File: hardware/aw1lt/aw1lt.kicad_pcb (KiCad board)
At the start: 2 copper layers, 30 x 22 mm, 27 parts, among them J1 ISP_FTDI, Q1 Q_NPN_CBE, SW1 SW_Push, SW2 SW_Push, SW3 SW_Push, U1 DS3231MZ, U2 ATMEGA328P-AU

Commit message: still trying to figure out this routing and placement...
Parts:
- C2, C3, C4, C7, R2: moved to B.Cu
- moved C9 15.0 mm to (126.6, 128.6)
- moved C8 12.5 mm to (127.4, 131.6), turned to 180 degrees
- moved C1 11.1 mm to (152.4, 137.2), turned to 180 degrees
- moved C10 10.8 mm to (126.2, 140.8)
- moved C3 8.94 mm to (148.2, 145.8), turned to 180 degrees
- moved C4 8.62 mm to (139.2, 145.8), turned to 180 degrees
- moved R2 8.30 mm to (132.4, 145.6)
- moved C2 8.20 mm to (144.4, 145.8)
- moved C7 7.79 mm to (127.2, 144.4), turned to 90 degrees
- moved R1 6.00 mm to (145.2, 131.8), turned to 0 degrees
- moved C6 3.20 mm to (127.2, 141.8), turned to 270 degrees
- moved U2 1.61 mm to (135.2, 132.4), turned to 0 degrees
- moved SW3 1.60 mm to (152.6, 142.0)
- moved SW1 1.00 mm to (127.4, 136.0)
- moved RN1 1.00 mm to (143.8, 135.2)
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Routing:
- net SCL: track 13.7 -> 0.00 mm
- net PB0: track 13.5 -> 0.00 mm
- net SDA: track 13.1 -> 0.00 mm
- net Net-(C6-Pad1): track 0.00 -> 7.65 mm
- net Net-(C2-Pad2): track 0.00 -> 7.48 mm, vias 0 -> 1
- net Net-(C2-Pad1): track 0.00 -> 6.35 mm, vias 0 -> 1
- net INT0: track 5.00 -> 0.00 mm
- net Net-(C3-Pad2): track 0.00 -> 4.96 mm, vias 0 -> 1
- net Net-(C3-Pad1): track 0.00 -> 4.54 mm, vias 0 -> 1
- net PB1: track 2.20 -> 0.00 mm
- net PB2: track 2.23 -> 0.11 mm

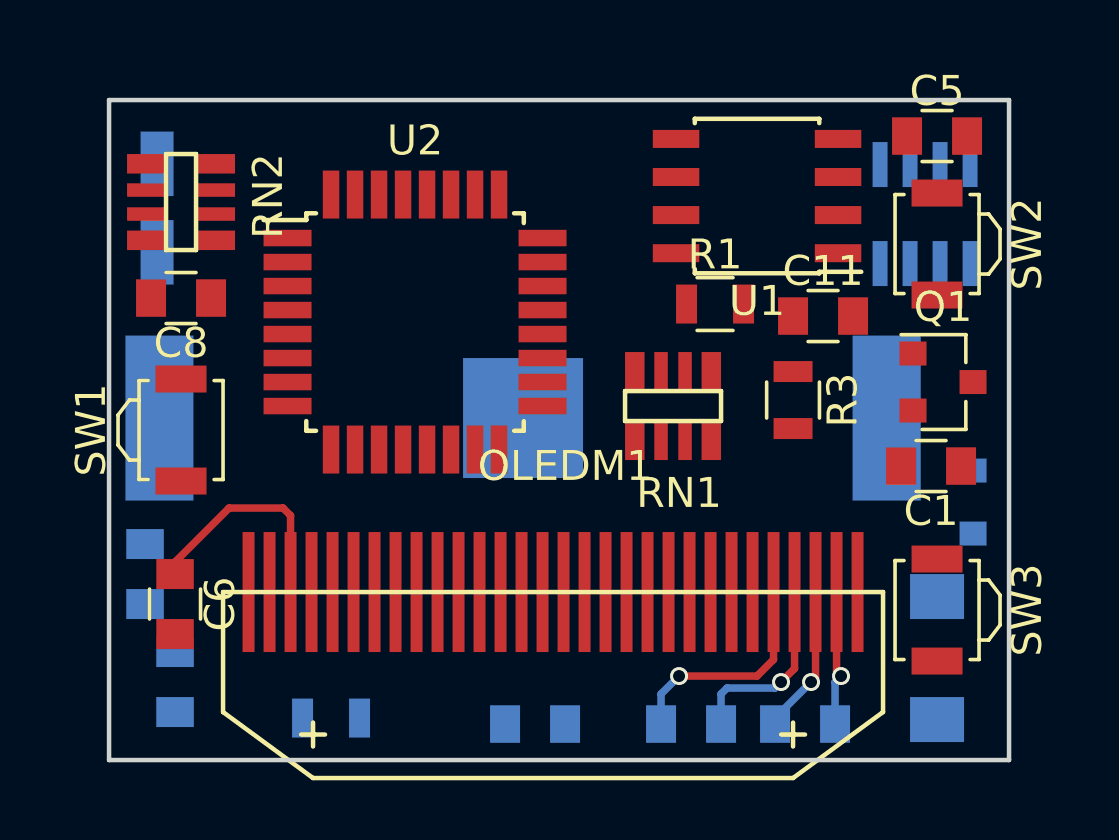
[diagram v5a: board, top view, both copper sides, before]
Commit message: made the coin cell footprint more accurate, did some measurements so that i know how far the actual coin battery will be protruding from the retainer and where i can place components
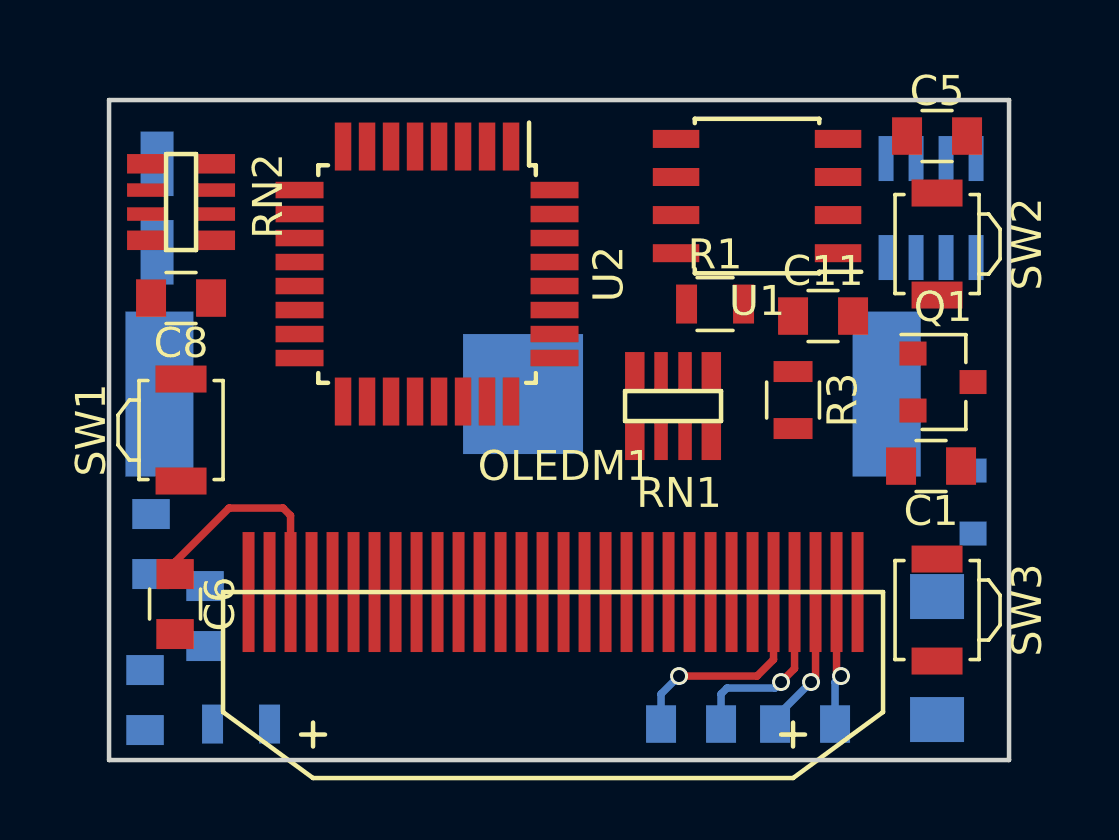
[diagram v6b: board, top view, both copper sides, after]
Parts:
- moved C4 11.6 mm to (128.2, 142.2), turned to 270 degrees
- moved R2 3.01 mm to (129.4, 145.8), turned to 180 degrees
- moved U2 1.65 mm to (135.6, 130.8), turned to 270 degrees
- moved C7 1.17 mm to (126.2, 145.0), turned to 270 degrees
- moved C10 1.02 mm to (126.4, 139.8)
- moved BT1 0.80 mm to (138.8, 134.8), turned to 180 degrees
- moved J1 0.28 mm to (152.4, 128.6)

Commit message: working on routing
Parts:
- moved C4 26.7 mm to (153.8, 134.6)
- moved R3 1.08 mm to (148.2, 136.0)
- moved C11 1.02 mm to (149.0, 133.2)
- moved RN1 0.72 mm to (144.2, 135.8)
- moved C7 0.45 mm to (126.4, 144.6)
- moved C2 0.40 mm to (144.8, 145.8)
- moved C3 0.40 mm to (148.6, 145.8)
- moved C10 0.28 mm to (126.2, 140.0)
- moved R1 0.20 mm to (145.4, 131.8)
- moved R2 0.20 mm to (129.4, 145.6)
- moved C8 0.20 mm to (127.2, 131.6)
- moved U1 0.20 mm to (146.6, 128.0)
- turned C9 to 90 degrees
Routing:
- net INT0: track 0.00 -> 16.0 mm, vias 0 -> 2
- net SPKR: track 0.00 -> 13.2 mm
- net Net-(C11-Pad1): track 0.00 -> 13.1 mm, vias 0 -> 3
- net SDA: track 0.00 -> 12.5 mm, vias 0 -> 2
- net SCL: track 0.00 -> 10.0 mm
- net Net-(C2-Pad2): track 7.48 -> 0.00 mm, vias 1 -> 0
- net Net-(C2-Pad1): track 6.35 -> 0.00 mm, vias 1 -> 0
- net Net-(C3-Pad2): track 4.96 -> 0.00 mm, vias 1 -> 0
- net Net-(C3-Pad1): track 4.54 -> 0.00 mm, vias 1 -> 0
- net PB2: track 0.11 -> 2.94 mm
- net PB1: track 0.00 -> 2.80 mm
- net PB0: track 0.00 -> 2.80 mm

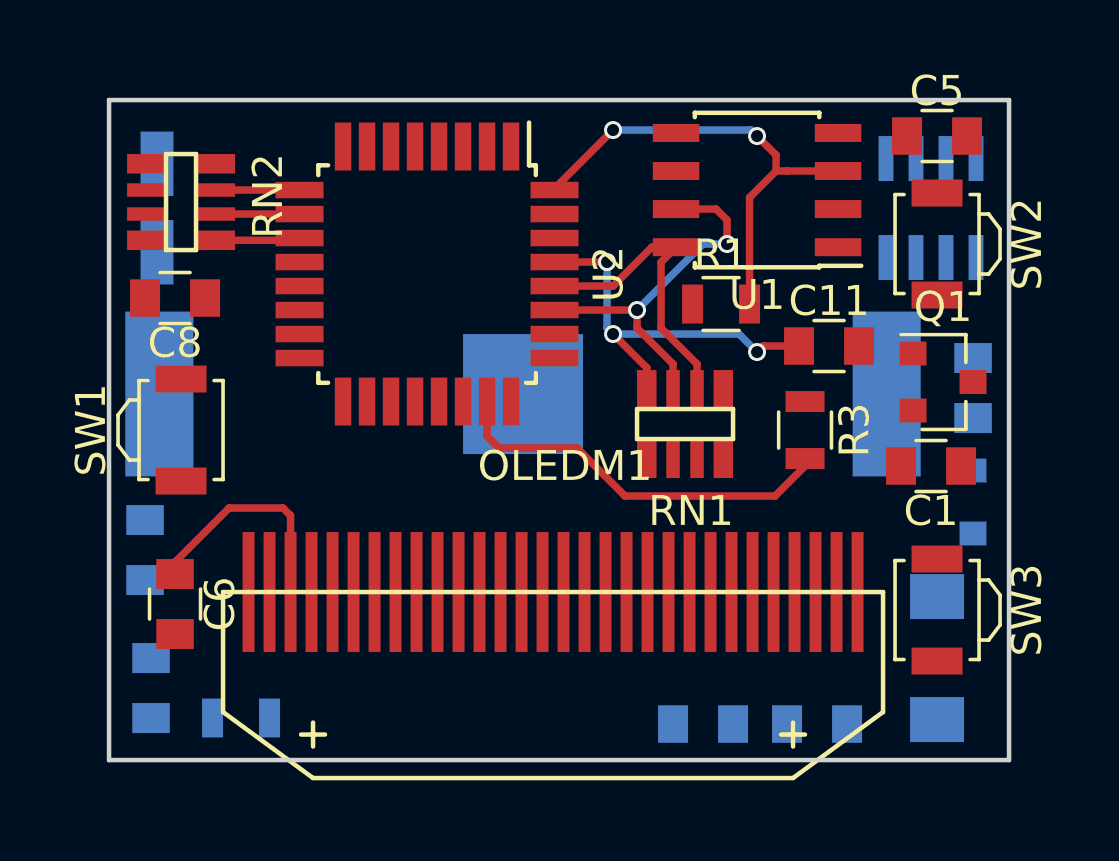
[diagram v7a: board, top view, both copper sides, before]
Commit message: working on more routing, switched to 603 on most caps and resistors for more space. thinking of rotating the micro for better pin location...
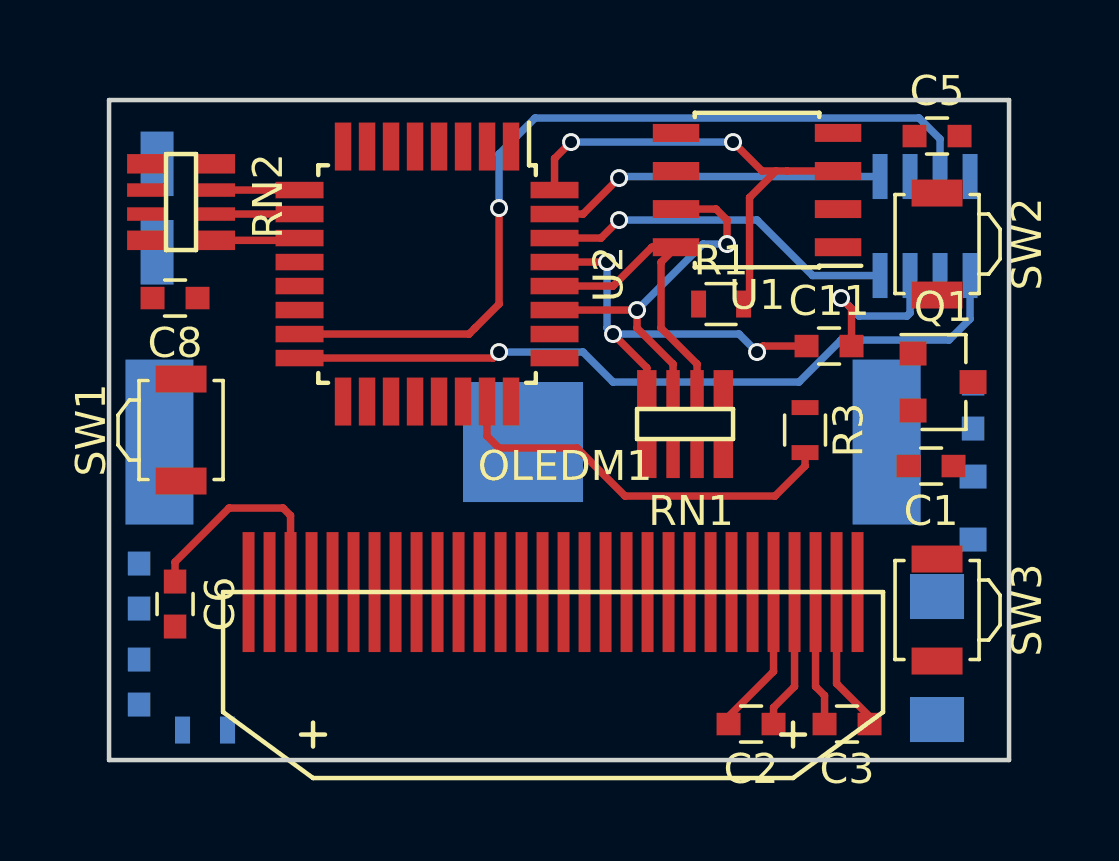
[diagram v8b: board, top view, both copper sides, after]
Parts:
- C1, C10, C11, C4, C5, C6, C7, C8: footprint Capacitors_SMD:C_0805 -> Capacitors_SMD:C_0603
- C2, C3: footprint Capacitors_SMD:C_0805 -> Capacitors_SMD:C_0603; moved to F.Cu
- R1, R2, R3: footprint Resistors_SMD:R_0805 -> Resistors_SMD:R_0603
- moved BT1 1.60 mm to (138.8, 136.4)
- moved C2 1.60 mm to (146.4, 145.8)
- moved R2 1.26 mm to (128.2, 146.0)
- moved C10 1.22 mm to (126.0, 141.2)
- moved C3 1.00 mm to (149.6, 145.8)
- moved J1 0.63 mm to (152.2, 129.2), turned to 90 degrees
- moved C4 0.60 mm to (153.8, 135.2), turned to 90 degrees
- moved C7 0.45 mm to (126.0, 144.4)
- moved D1 0.20 mm to (153.8, 138.6)
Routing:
- net MOSI: track 0.00 -> 28.8 mm, vias 0 -> 1
- net MISO: track 0.00 -> 25.2 mm, vias 0 -> 1
- net RXD: track 0.00 -> 11.9 mm, vias 0 -> 1
- net TXD: track 0.00 -> 11.4 mm, vias 0 -> 1
- net DTR: track 0.00 -> 5.58 mm, vias 0 -> 1
- net Net-(C2-Pad2): track 0.00 -> 5.02 mm
- net Net-(C3-Pad1): track 0.00 -> 4.86 mm
- net Net-(C2-Pad1): track 0.00 -> 4.69 mm
- net Net-(C3-Pad2): track 0.00 -> 4.52 mm
